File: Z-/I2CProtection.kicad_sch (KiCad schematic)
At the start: 9 parts, among them Q1 NX3008NBKS, Q2 MBT2222ADW1T1

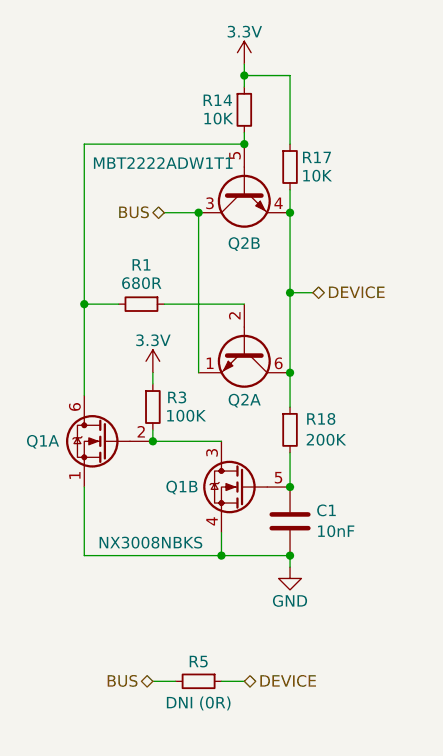
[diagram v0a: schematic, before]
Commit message: Moved burnwire around and added switch to coil driver
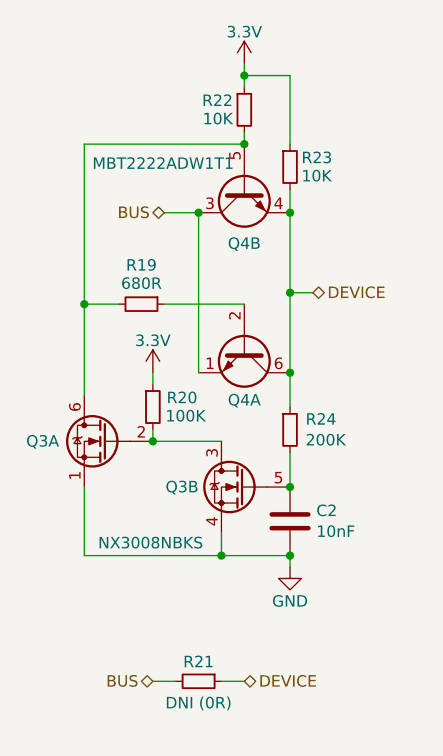
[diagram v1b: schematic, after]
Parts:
- C2: renamed from C1; symbol SolarPanels:C -> Device:C
- Q3: renamed from Q1; symbol SolarPanels:NX3008NBKS -> Argus-Miscellaneous:NX3008NBKS
- Q4: renamed from Q2; symbol SolarPanels:MBT2222ADW1T1 -> Transistor_BJT:MBT2222ADW1T1
- R19: renamed from R1; symbol SolarPanels:R_Small -> Device:R_Small
- R20: renamed from R3; symbol SolarPanels:R_Small -> Device:R_Small
- R21: renamed from R5; symbol SolarPanels:R_Small -> Device:R_Small
- R22: renamed from R14; symbol SolarPanels:R_Small -> Device:R_Small
- R23: renamed from R17; symbol SolarPanels:R_Small -> Device:R_Small
- R24: renamed from R18; symbol SolarPanels:R_Small -> Device:R_Small
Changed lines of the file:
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@@
 	)
 	(symbol
-		(lib_id "SolarPanels:R_Small")
+		(lib_id "Device:R_Small")
 		(at 148.59 57.15 0)
 		(unit 1)
@@
 		(on_board yes)
 		(dnp no)
-		(property "Reference" "R14"
+		(property "Reference" "R22"
 			(at 147.32 56.134 0)
 			(effects
@@
 	)
 	(symbol
-		(lib_id "SolarPanels:NX3008NBKS")
+		(lib_id "Argus-Miscellaneous:NX3008NBKS")
 		(at 147.32 99.06 0)
 		(mirror y)
@@
 		(on_board yes)
 		(dnp no)
-		(property "Reference" "Q1"
+		(property "Reference" "Q3"
 			(at 143.51 99.06 0)
 			(effects
@@
 	)
 	(symbol
-		(lib_id "SolarPanels:R_Small")
+		(lib_id "Device:R_Small")
 		(at 137.16 78.74 270)
 		(unit 1)
@@
 		(on_board yes)
 		(dnp no)
-		(property "Reference" "R1"
+		(property "Reference" "R19"
 			(at 137.16 74.422 90)
 			(effects
@@
 		(on_board yes)
 		(dnp no)
-		(property "Reference" "#PWR01"
+		(property "Reference" "#PWR02"
 			(at 153.67 114.3 0)
 			(effects
@@
 			)
 		)
-		(property "Description" ""
+		(property "Description" "Power symbol creates a global label with name \"GND\" , ground"
 			(at 153.67 107.95 0)
 			(effects
@@
 	)
 	(symbol
-		(lib_id "SolarPanels:R_Small")
+		(lib_id "Device:R_Small")
 		(at 143.51 120.65 270)
 		(unit 1)
@@
 		(on_board yes)
 		(dnp no)
-		(property "Reference" "R5"
+		(property "Reference" "R21"
 			(at 143.51 118.491 90)
 			(effects
@@
 	)
 	(symbol
-		(lib_id "SolarPanels:C")
+		(lib_id "Device:C")
 		(at 153.67 102.87 0)
 		(unit 1)
@@
 		(on_board yes)
 		(dnp no)
-		(property "Reference" "C1"
+		(property "Reference" "C2"
 			(at 156.591 101.7016 0)
 			(effects
@@
 	)
 	(symbol
-		(lib_id "SolarPanels:MBT2222ADW1T1")
+		(lib_id "Transistor_BJT:MBT2222ADW1T1")
 		(at 148.59 66.04 90)
 		(mirror x)
@@
 		(on_board yes)
 		(dnp no)
-		(property "Reference" "Q2"
+		(property "Reference" "Q4"
 			(at 148.59 72.009 90)
 			(effects
@@
 	)
 	(symbol
-		(lib_id "SolarPanels:R_Small")
+		(lib_id "Device:R_Small")
 		(at 153.67 92.71 0)
 		(unit 1)
@@
 		(on_board yes)
 		(dnp no)
-		(property "Reference" "R18"
+		(property "Reference" "R24"
 			(at 155.3972 91.5416 0)
 			(effects
@@
 	)
 	(symbol
-		(lib_id "SolarPanels:NX3008NBKS")
+		(lib_id "Argus-Miscellaneous:NX3008NBKS")
 		(at 132.08 93.98 0)
 		(mirror y)
@@
 		(on_board yes)
 		(dnp no)
-		(property "Reference" "Q1"
+		(property "Reference" "Q3"
 			(at 128.016 93.98 0)
 			(effects
@@
 		(on_board yes)
 		(dnp no)
-		(property "Reference" "#SUPPLY02"
+		(property "Reference" "#SUPPLY04"
 			(at 138.43 86.36 0)
 			(effects
@@
 	)
 	(symbol
-		(lib_id "SolarPanels:R_Small")
+		(lib_id "Device:R_Small")
 		(at 138.43 90.17 0)
 		(unit 1)
@@
 		(on_board yes)
 		(dnp no)
-		(property "Reference" "R3"
+		(property "Reference" "R20"
 			(at 139.954 89.154 0)
 			(effects
@@
 	)
 	(symbol
-		(lib_id "SolarPanels:R_Small")
+		(lib_id "Device:R_Small")
 		(at 153.67 63.5 0)
 		(unit 1)
@@
 		(on_board yes)
 		(dnp no)
-		(property "Reference" "R17"
+		(property "Reference" "R23"
 			(at 154.94 62.484 0)
 			(effects
@@
 	)
 	(symbol
-		(lib_id "SolarPanels:MBT2222ADW1T1")
+		(lib_id "Transistor_BJT:MBT2222ADW1T1")
 		(at 148.59 83.82 270)
 		(unit 1)
@@
 		(on_board yes)
 		(dnp no)
-		(property "Reference" "Q2"
+		(property "Reference" "Q4"
 			(at 148.59 89.408 90)
 			(effects
@@
 		(on_board yes)
 		(dnp no)
-		(property "Reference" "#SUPPLY03"
+		(property "Reference" "#SUPPLY05"
 			(at 148.59 52.07 0)
 			(effects

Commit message: temp
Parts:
- removed C2: 10nF, Capacitor_SMD:C_0603_1608Metric, symbol Device:C
- removed Q3: NX3008NBKS, Package_TO_SOT_SMD:SOT-363_SC-70-6, symbol Argus-Miscellaneous:NX3008NBKS
- removed Q4: MBT2222ADW1T1, Package_TO_SOT_SMD:SOT-363_SC-70-6, symbol Transistor_BJT:MBT2222ADW1T1
- removed R19: 680R, Resistor_SMD:R_0603_1608Metric, symbol Device:R_Small
- removed R20: 100K, Resistor_SMD:R_0603_1608Metric, symbol Device:R_Small
- removed R21: DNI (0R), Resistor_SMD:R_0603_1608Metric, symbol Device:R_Small
- removed R22, R23: 10K, Resistor_SMD:R_0603_1608Metric, symbol Device:R_Small
- removed R24: 200K, Resistor_SMD:R_0603_1608Metric, symbol Device:R_Small
- added C1: 10nF, Capacitor_SMD:C_0603_1608Metric, symbol Device:C
- added Q1: NX3008NBKS, Package_TO_SOT_SMD:SOT-363_SC-70-6, symbol Argus-Miscellaneous:NX3008NBKS
- added Q2: MBT2222ADW1T1, Package_TO_SOT_SMD:SOT-363_SC-70-6, symbol Transistor_BJT:MBT2222ADW1T1
- added R1: 680R, Resistor_SMD:R_0603_1608Metric, symbol Device:R_Small
- added R14, R17: 10K, Resistor_SMD:R_0603_1608Metric, symbol Device:R_Small
- added R18: 200K, Resistor_SMD:R_0603_1608Metric, symbol Device:R_Small
- added R3: 100K, Resistor_SMD:R_0603_1608Metric, symbol Device:R_Small
- added R5: DNI (0R), Resistor_SMD:R_0603_1608Metric, symbol Device:R_Small
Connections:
- net BUS: now also Q2.1 (E1), Q2.3 (C2), R5.2
- net DEVICE: now also Q2.4 (E2), Q2.6 (C1), R17.2, R18.1, R5.1
- net GND: now also C1.2, Q1.1 (S2), Q1.4 (S1)
- new net: Q1.6 (D1), Q2.5 (B2), R1.2, R14.2
- new net: Q2.2 (B1), R1.1
- new net: C1.1, Q1.5 (G1), R18.2
- new net: Q1.2 (G2), Q1.3 (D2), R3.2
- new net VDD: R14.1, R17.1, R3.1

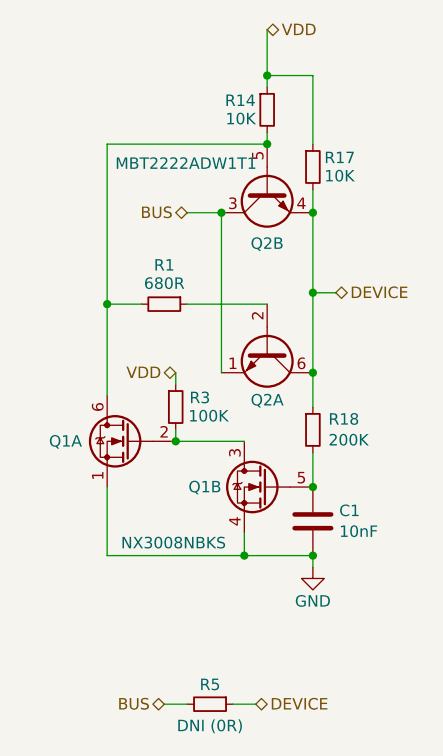
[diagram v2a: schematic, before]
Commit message: Updated schematics/layout with mainboard compatability
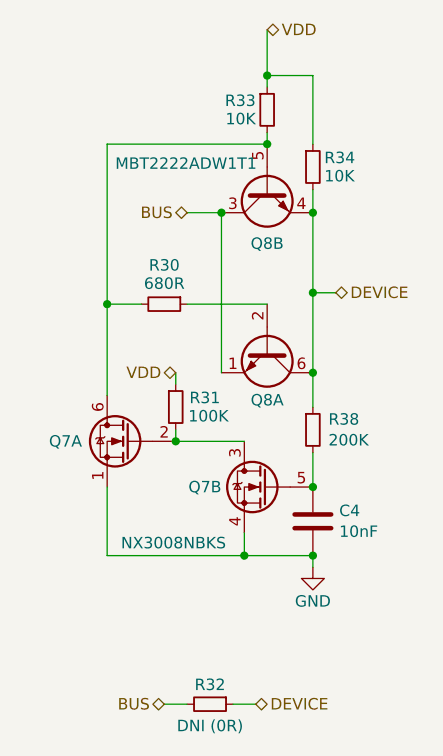
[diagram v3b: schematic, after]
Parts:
- renumbered C1 to C4, Q1 to Q7, Q2 to Q8, R1 to R30, R3 to R31, R5 to R32, R14 to R33, R17 to R34, R18 to R38
